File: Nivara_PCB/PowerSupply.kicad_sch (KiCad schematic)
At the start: 6 parts, among them U2 AP63203WU

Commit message: Actualización del pcb
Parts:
- C1: renamed from C3; value C_1206 -> 10uF
- renumbered C4 to C2, C2 to C3, C6 to C5
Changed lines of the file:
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@@
 		(dnp no)
 		(fields_autoplaced yes)
-		(property "Reference" "C6"
+		(property "Reference" "C5"
 			(at 127 57.1499 0)
 			(effects
@@
 			(project "Nivara_PCB"
 				(path "/13184db0-a71d-4054-b13a-bbf46d2b100d/4e7fa7f2-8bf5-4f9c-874d-fa1b4fd76f92/c8cd749e-9134-4d76-b8ef-ce0eb3eb606f"
-					(reference "C6")
+					(reference "C5")
 					(unit 1)
 				)
@@
 		(dnp no)
 		(fields_autoplaced yes)
-		(property "Reference" "C3"
+		(property "Reference" "C1"
 			(at 57.15 57.1499 0)
 			(effects
@@
 			)
 		)
-		(property "Value" "C_1206"
+		(property "Value" "10uF"
 			(at 57.15 59.6899 0)
 			(effects
@@
 			(project ""
 				(path "/13184db0-a71d-4054-b13a-bbf46d2b100d/4e7fa7f2-8bf5-4f9c-874d-fa1b4fd76f92/c8cd749e-9134-4d76-b8ef-ce0eb3eb606f"
-					(reference "C3")
+					(reference "C1")
 					(unit 1)
 				)
@@
 		(dnp no)
 		(fields_autoplaced yes)
-		(property "Reference" "C2"
+		(property "Reference" "C3"
 			(at 87.63 41.91 90)
 			(effects
@@
 			(project "Nivara_PCB"
 				(path "/13184db0-a71d-4054-b13a-bbf46d2b100d/4e7fa7f2-8bf5-4f9c-874d-fa1b4fd76f92/c8cd749e-9134-4d76-b8ef-ce0eb3eb606f"
-					(reference "C2")
+					(reference "C3")
 					(unit 1)
 				)
@@
 		(dnp no)
 		(fields_autoplaced yes)
-		(property "Reference" "C4"
+		(property "Reference" "C2"
 			(at 114.3 57.1499 0)
 			(effects
@@
 			(project "Nivara_PCB"
 				(path "/13184db0-a71d-4054-b13a-bbf46d2b100d/4e7fa7f2-8bf5-4f9c-874d-fa1b4fd76f92/c8cd749e-9134-4d76-b8ef-ce0eb3eb606f"
-					(reference "C4")
-					(unit 1)
-				)
+					(reference "C2")
+					(unit 1)
+				)

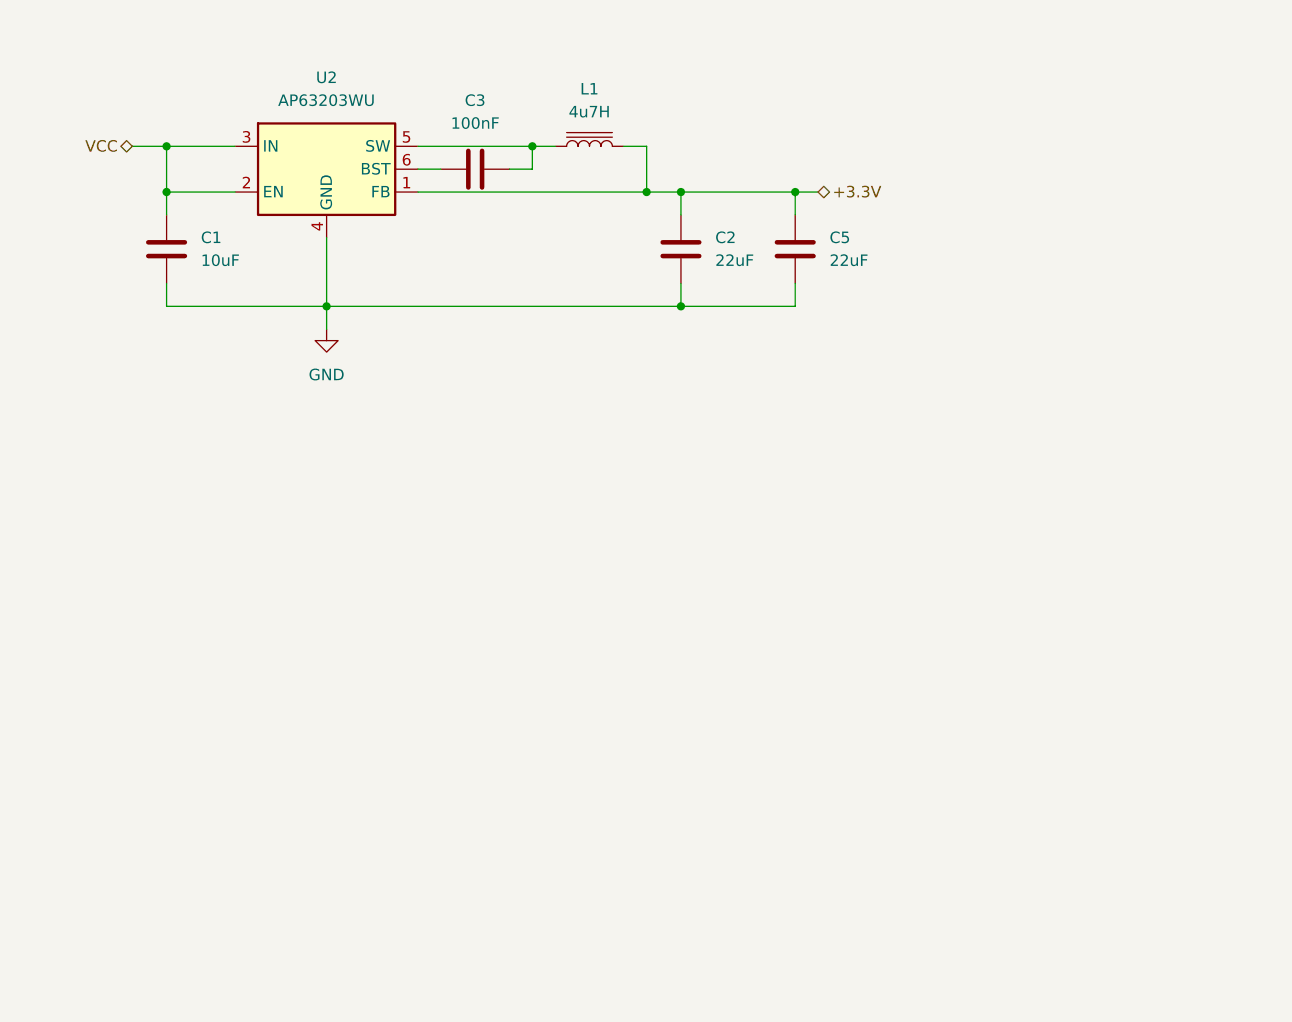
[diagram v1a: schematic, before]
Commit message: Fuente de 12V para activar optoacopladores y relés
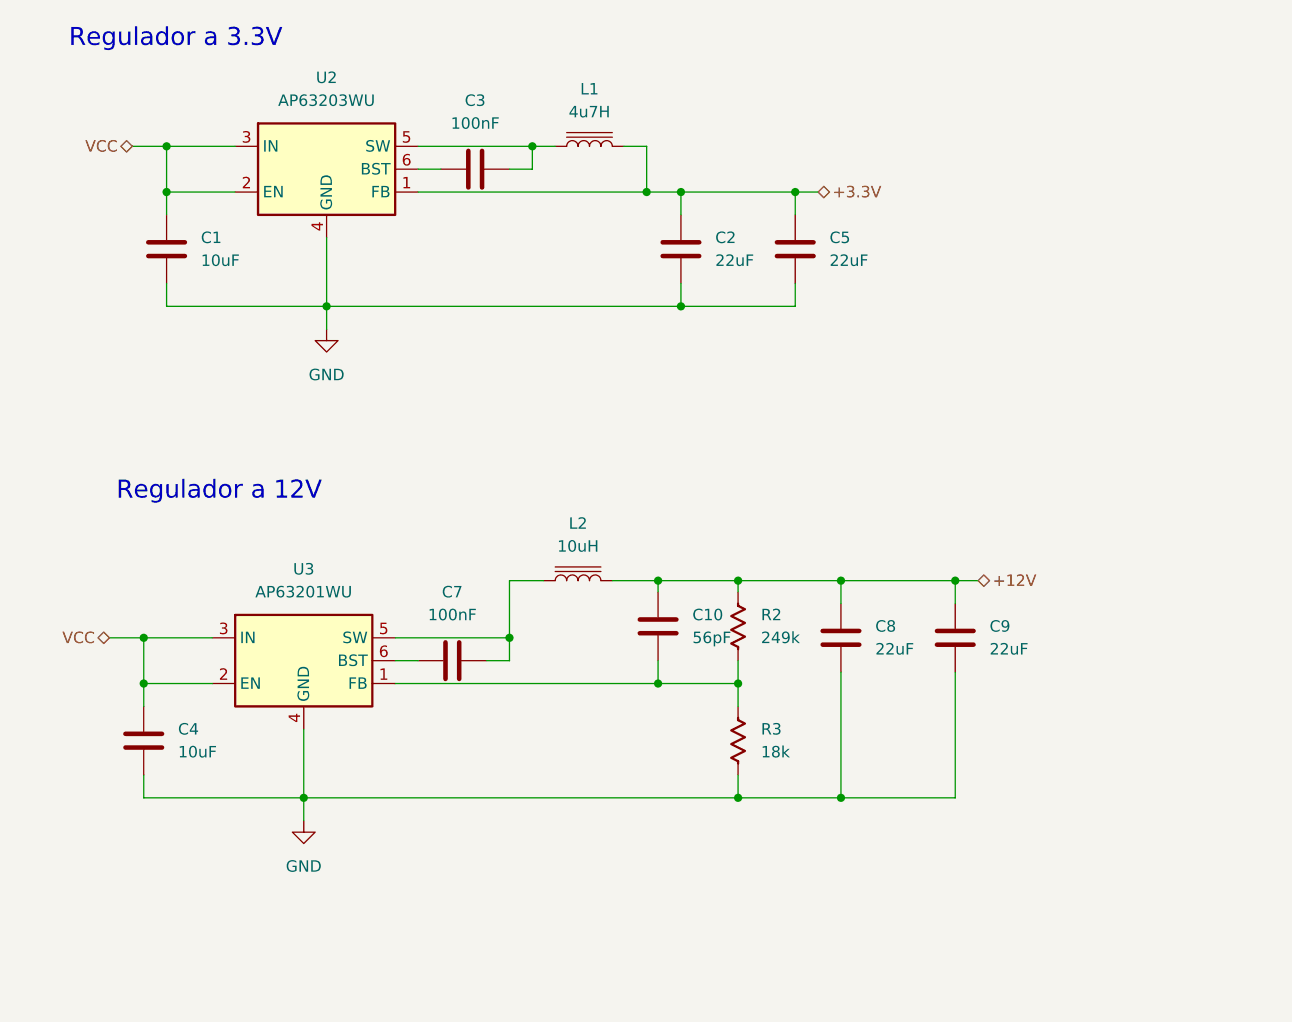
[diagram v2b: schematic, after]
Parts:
- added C10: 56pF, PCM_Capacitor_SMD_AKL:C_0805_2012Metric, symbol PCM_Capacitor_AKL:C_0805
- added C4: 10uF, PCM_Capacitor_SMD_AKL:C_1206_3216Metric, symbol PCM_Capacitor_AKL:C_1206
- added C7: 100nF, PCM_Capacitor_SMD_AKL:C_0805_2012Metric, symbol PCM_Capacitor_AKL:C_0805
- added C8, C9: 22uF, PCM_Capacitor_SMD_AKL:C_0805_2012Metric, symbol PCM_Capacitor_AKL:C_0805
- added L2: 10uH, Inductor_SMD:L_APV_ANR6028, symbol Device:L_Iron
- added R2: 249k, PCM_Resistor_SMD_AKL:R_0603_1608Metric, symbol PCM_Resistor_US_AKL:R_0603
- added R3: 18k, PCM_Resistor_SMD_AKL:R_0603_1608Metric, symbol PCM_Resistor_US_AKL:R_0603
- added U3: AP63201WU, Package_TO_SOT_SMD:TSOT-23-6, symbol Regulator_Switching:AP63201WU
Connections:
- net GND: now also C4.2, C8.2, C9.2, R3.2, U3.4 (GND)
- net VCC: now also C4.1, U3.2 (EN), U3.3 (IN)
- new net: C7.2, L2.1, U3.5 (SW)
- new net: C10.2, R2.2, R3.1, U3.1 (FB)
- new net: C7.1, U3.6 (BST)
- new net +12V: C10.1, C8.1, C9.1, L2.2, R2.1
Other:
- note added: "Regulador a 12V"
- note added: "Regulador a 3.3V"

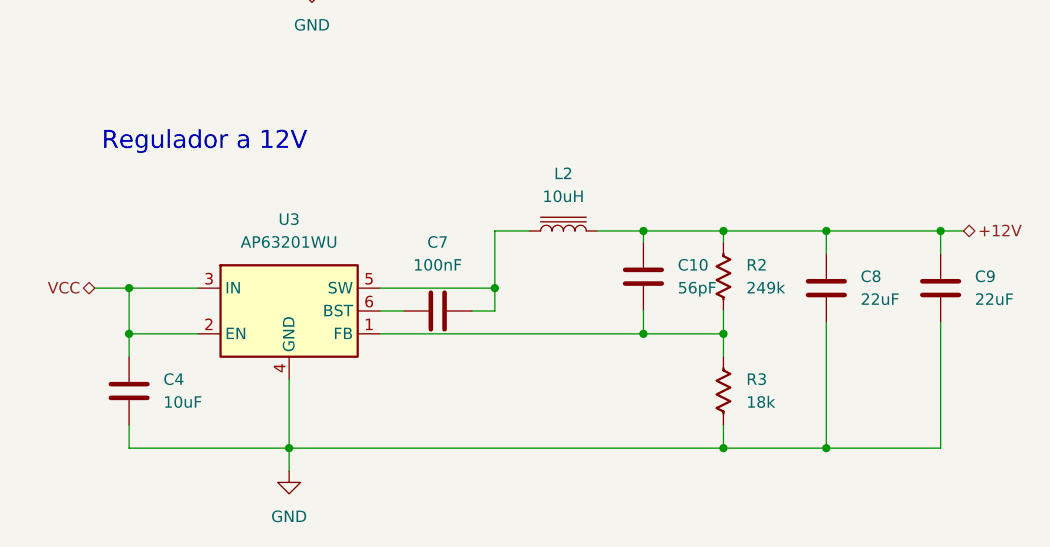
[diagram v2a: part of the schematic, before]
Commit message: Cambio a fuente de 5V para utilizar reles HF49FD Es mejor utilizar una fuente de 5V para alimentar los reles y los periféricos en general, que 12V
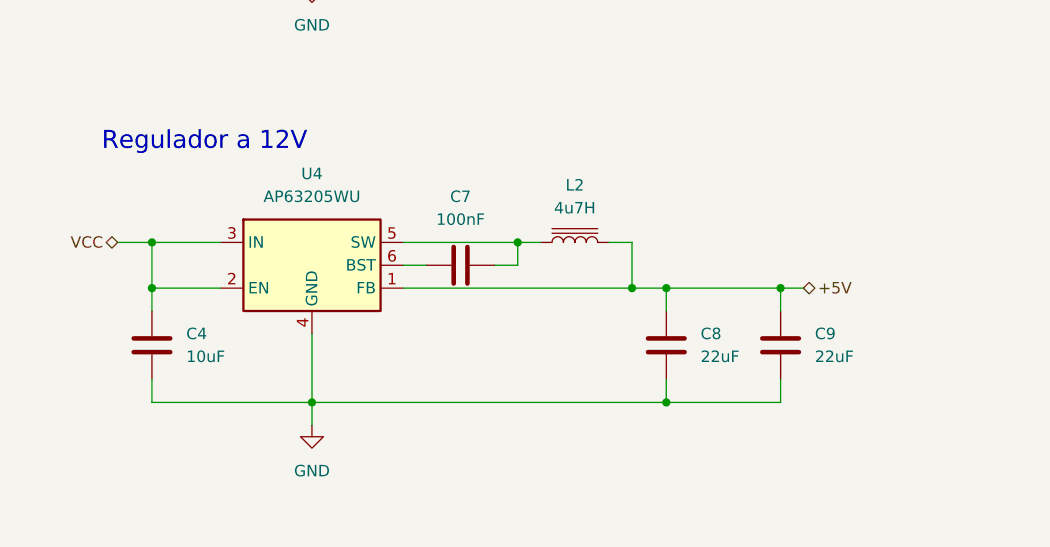
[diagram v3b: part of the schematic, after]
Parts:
- removed C10: 56pF, PCM_Capacitor_SMD_AKL:C_0805_2012Metric, symbol PCM_Capacitor_AKL:C_0805
- removed R2: 249k, PCM_Resistor_SMD_AKL:R_0603_1608Metric, symbol PCM_Resistor_US_AKL:R_0603
- removed R3: 18k, PCM_Resistor_SMD_AKL:R_0603_1608Metric, symbol PCM_Resistor_US_AKL:R_0603
- removed U3: AP63201WU, Package_TO_SOT_SMD:TSOT-23-6, symbol Regulator_Switching:AP63201WU
- added U4: AP63205WU, Package_TO_SOT_SMD:TSOT-23-6, symbol Regulator_Switching:AP63205WU
- L2: value 10uH -> 4u7H
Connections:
- net GND: now also U4.4 (GND)
- net VCC: now also U4.2 (EN), U4.3 (IN)
- net at C7.2, L2.1: now also U4.5 (SW)
- net at C7.1: now also U4.6 (BST)
- net +12V renamed +5V
- net +5V: now also U4.1 (FB)

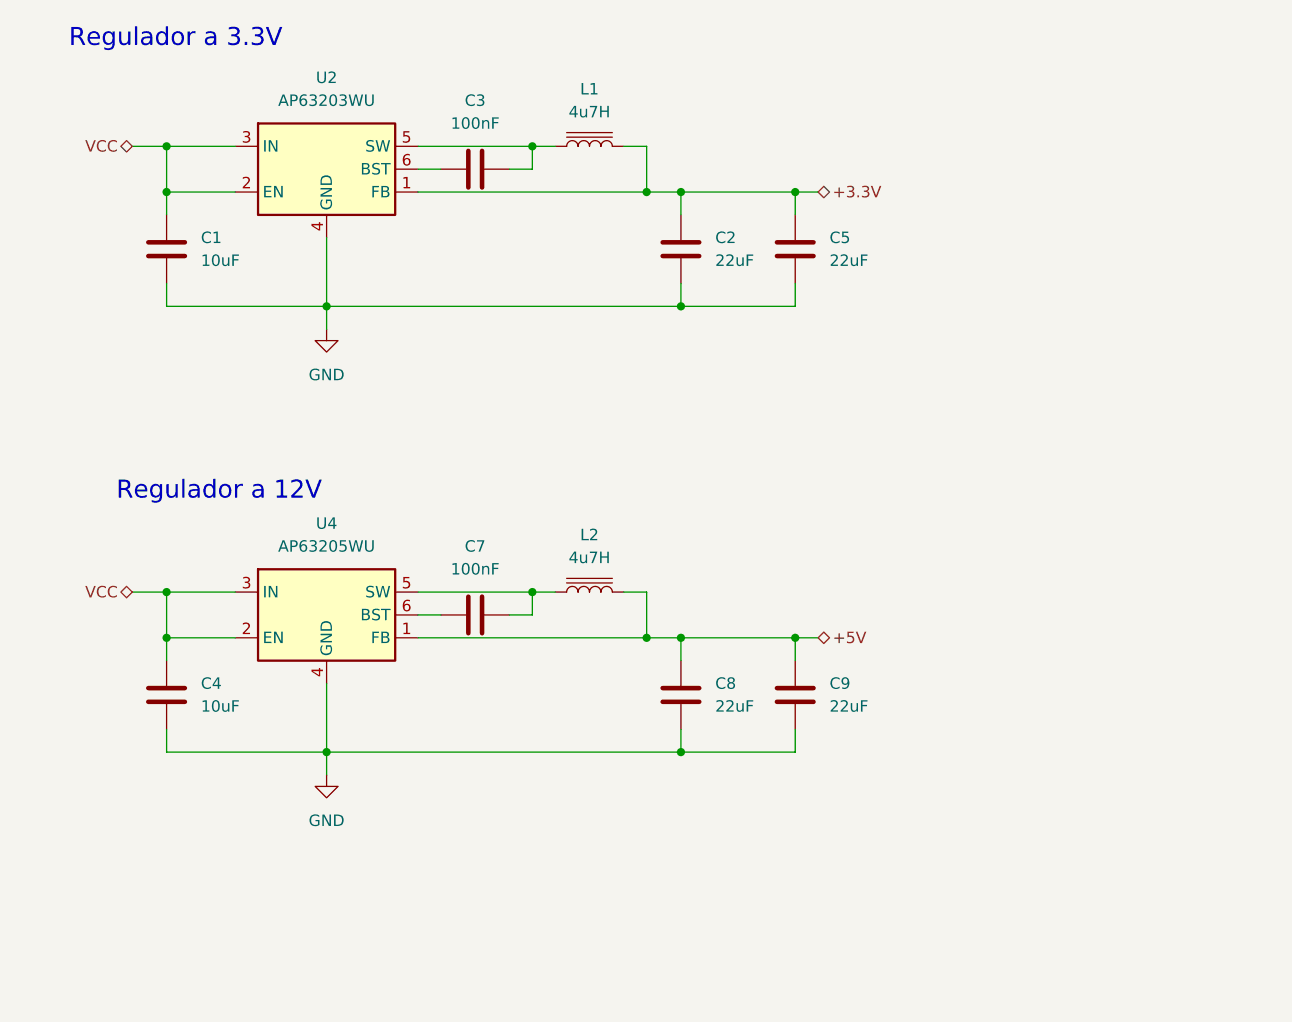
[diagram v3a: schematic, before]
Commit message: Añadido de funciones NPN/PNP
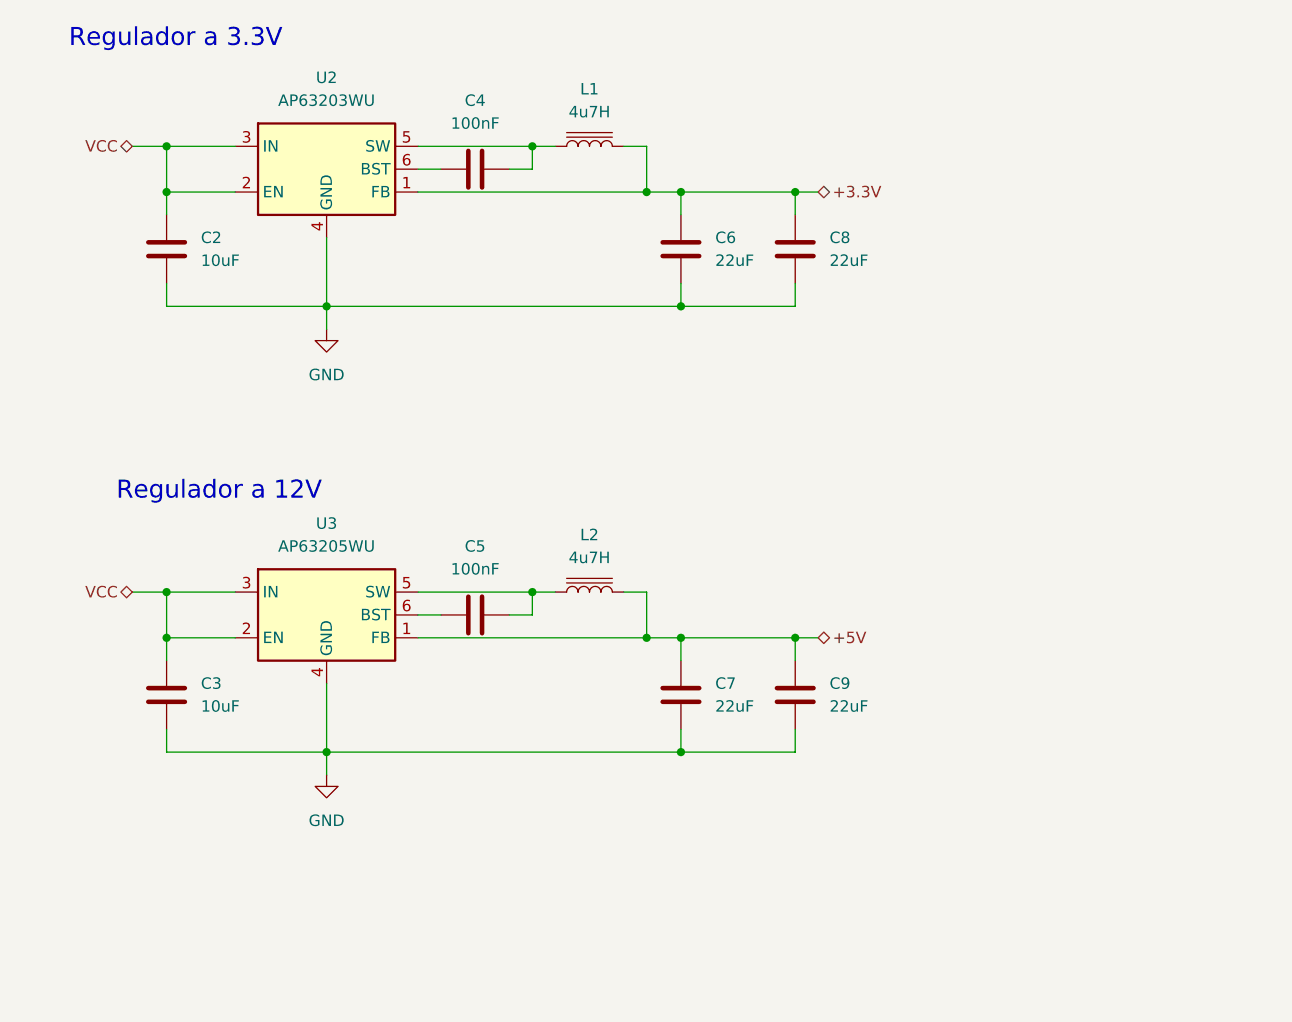
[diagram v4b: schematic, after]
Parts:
- renumbered C1 to C2, C4 to C3, C3 to C4, C7 to C5, C2 to C6, C8 to C7, C5 to C8, U4 to U3
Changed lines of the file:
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@@
 		(dnp no)
 		(fields_autoplaced yes)
-		(property "Reference" "#PWR014"
+		(property "Reference" "#PWR015"
 			(at 71.12 123.19 0)
 			(effects
@@
 			(project "Nivara_PCB"
 				(path "/13184db0-a71d-4054-b13a-bbf46d2b100d/4e7fa7f2-8bf5-4f9c-874d-fa1b4fd76f92/c8cd749e-9134-4d76-b8ef-ce0eb3eb606f"
-					(reference "#PWR014")
+					(reference "#PWR015")
 					(unit 1)
 				)
@@
 		(dnp no)
 		(fields_autoplaced yes)
-		(property "Reference" "C5"
+		(property "Reference" "C8"
 			(at 127 57.1499 0)
 			(effects
@@
 			(project "Nivara_PCB"
 				(path "/13184db0-a71d-4054-b13a-bbf46d2b100d/4e7fa7f2-8bf5-4f9c-874d-fa1b4fd76f92/c8cd749e-9134-4d76-b8ef-ce0eb3eb606f"
-					(reference "C5")
+					(reference "C8")
 					(unit 1)
 				)
@@
 		(dnp no)
 		(fields_autoplaced yes)
-		(property "Reference" "C1"
+		(property "Reference" "C2"
 			(at 57.15 57.1499 0)
 			(effects
@@
 			(project ""
 				(path "/13184db0-a71d-4054-b13a-bbf46d2b100d/4e7fa7f2-8bf5-4f9c-874d-fa1b4fd76f92/c8cd749e-9134-4d76-b8ef-ce0eb3eb606f"
-					(reference "C1")
+					(reference "C2")
 					(unit 1)
 				)
@@
 		(dnp no)
 		(fields_autoplaced yes)
-		(property "Reference" "C4"
+		(property "Reference" "C3"
 			(at 57.15 106.6799 0)
 			(effects
@@
 			(project "Nivara_PCB"
 				(path "/13184db0-a71d-4054-b13a-bbf46d2b100d/4e7fa7f2-8bf5-4f9c-874d-fa1b4fd76f92/c8cd749e-9134-4d76-b8ef-ce0eb3eb606f"
-					(reference "C4")
+					(reference "C3")
 					(unit 1)
 				)
@@
 		(dnp no)
 		(fields_autoplaced yes)
-		(property "Reference" "U4"
+		(property "Reference" "U3"
 			(at 71.12 88.9 0)
 			(effects
@@
 			(project "Nivara_PCB"
 				(path "/13184db0-a71d-4054-b13a-bbf46d2b100d/4e7fa7f2-8bf5-4f9c-874d-fa1b4fd76f92/c8cd749e-9134-4d76-b8ef-ce0eb3eb606f"
-					(reference "U4")
+					(reference "U3")
 					(unit 1)
 				)
@@
 		(dnp no)
 		(fields_autoplaced yes)
-		(property "Reference" "C3"
+		(property "Reference" "C4"
 			(at 87.63 41.91 90)
 			(effects
@@
 			(project "Nivara_PCB"
 				(path "/13184db0-a71d-4054-b13a-bbf46d2b100d/4e7fa7f2-8bf5-4f9c-874d-fa1b4fd76f92/c8cd749e-9134-4d76-b8ef-ce0eb3eb606f"
-					(reference "C3")
+					(reference "C4")
 					(unit 1)
 				)
@@
 		(dnp no)
 		(fields_autoplaced yes)
-		(property "Reference" "#PWR04"
+		(property "Reference" "#PWR014"
 			(at 71.12 73.66 0)
 			(effects
@@
 			(project ""
 				(path "/13184db0-a71d-4054-b13a-bbf46d2b100d/4e7fa7f2-8bf5-4f9c-874d-fa1b4fd76f92/c8cd749e-9134-4d76-b8ef-ce0eb3eb606f"
-					(reference "#PWR04")
+					(reference "#PWR014")
 					(unit 1)
 				)
@@
 		(dnp no)
 		(fields_autoplaced yes)
-		(property "Reference" "C8"
+		(property "Reference" "C7"
 			(at 114.3 106.6799 0)
 			(effects
@@
 			(project "Nivara_PCB"
 				(path "/13184db0-a71d-4054-b13a-bbf46d2b100d/4e7fa7f2-8bf5-4f9c-874d-fa1b4fd76f92/c8cd749e-9134-4d76-b8ef-ce0eb3eb606f"
-					(reference "C8")
+					(reference "C7")
 					(unit 1)
 				)
@@
 		(dnp no)
 		(fields_autoplaced yes)
-		(property "Reference" "C2"
+		(property "Reference" "C6"
 			(at 114.3 57.1499 0)
 			(effects
@@
 			(project "Nivara_PCB"
 				(path "/13184db0-a71d-4054-b13a-bbf46d2b100d/4e7fa7f2-8bf5-4f9c-874d-fa1b4fd76f92/c8cd749e-9134-4d76-b8ef-ce0eb3eb606f"
-					(reference "C2")
+					(reference "C6")
 					(unit 1)
 				)
@@
 		(dnp no)
 		(fields_autoplaced yes)
-		(property "Reference" "C7"
+		(property "Reference" "C5"
 			(at 87.63 91.44 90)
 			(effects
@@
 			(project "Nivara_PCB"
 				(path "/13184db0-a71d-4054-b13a-bbf46d2b100d/4e7fa7f2-8bf5-4f9c-874d-fa1b4fd76f92/c8cd749e-9134-4d76-b8ef-ce0eb3eb606f"
-					(reference "C7")
-					(unit 1)
-				)
+					(reference "C5")
+					(unit 1)
+				)

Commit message: Cambios en archivos a subir
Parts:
- added TP1: +VCC, TestPoint:TestPoint_Pad_1.0x1.0mm, symbol Connector:TestPoint_Probe
- added TP2: +3.3V, TestPoint:TestPoint_Pad_1.0x1.0mm, symbol Connector:TestPoint_Probe
- added TP3: +5V, TestPoint:TestPoint_Pad_1.0x1.0mm, symbol Connector:TestPoint_Probe
- added TP4: GND, TestPoint:TestPoint_Pad_1.0x1.0mm, symbol Connector:TestPoint_Probe
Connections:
- net +3.3V: now also TP2.1
- net +5V: now also TP3.1
- net GND: now also TP4.1
- net VCC: now also TP1.1
